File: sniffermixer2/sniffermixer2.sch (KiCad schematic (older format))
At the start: 19 parts

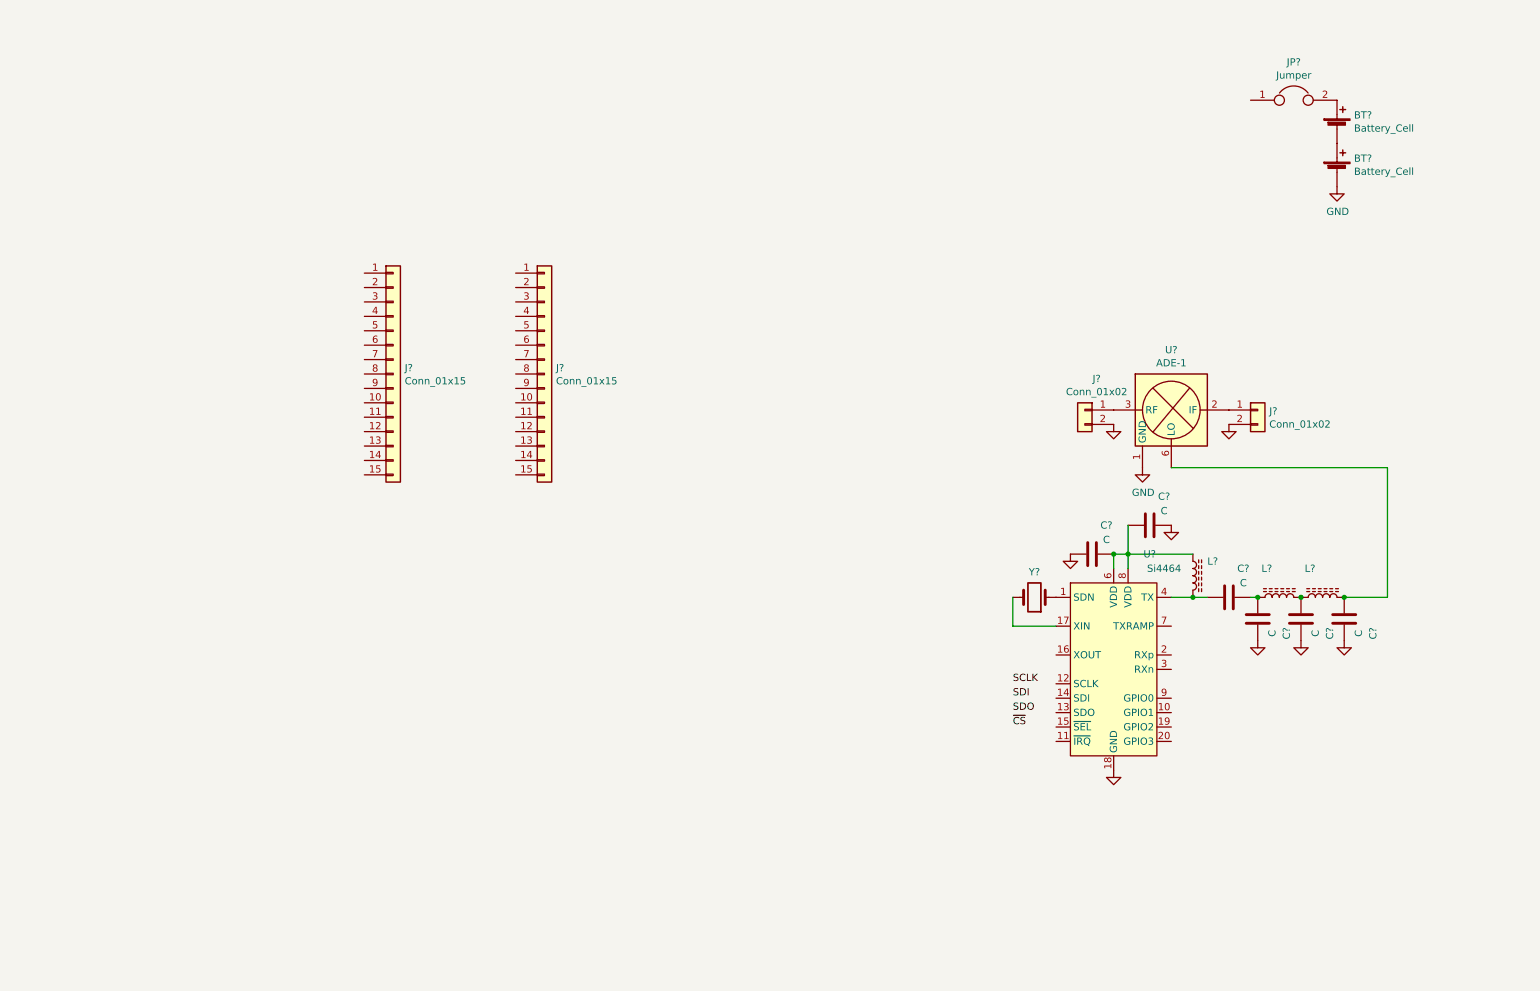
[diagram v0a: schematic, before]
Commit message: some minor schematic capture: dupe connectors, tricolor LED, wiring
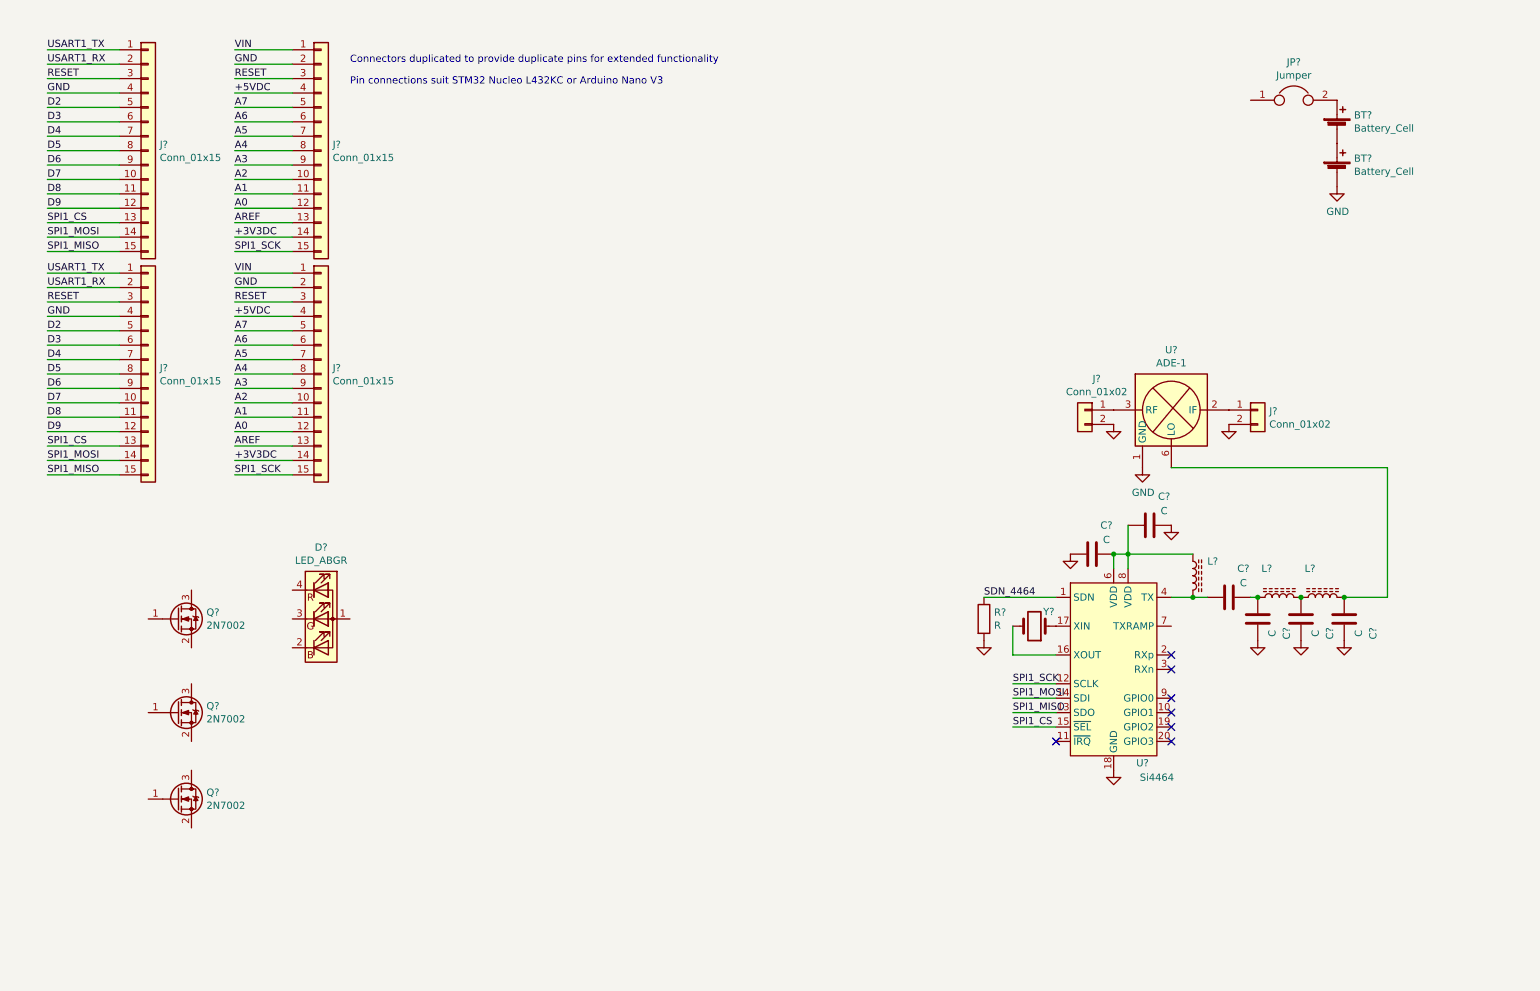
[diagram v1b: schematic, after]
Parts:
- added D?: LED_ABGR, symbol Device:LED_ABGR
- added J? (x2): Conn_01x15, symbol Connector_Generic:Conn_01x15
- added Q? (x3): 2N7002, Package_TO_SOT_SMD:SOT-23, symbol Transistor_FET:2N7002
- added R?: R, symbol Device:R
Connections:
- net GND: now also J?.2 (Pin_2), J?.4 (Pin_4), J?.2 (Pin_2), J?.4 (Pin_4), R?.2
- net at Y?.1: now also U?.17 (XIN); no longer U?.1 (SDN)
- net SPI1_SCK: now reaches U?.12 (SCLK)
- net SPI1_SCK: now also J?.15 (Pin_15), J?.15 (Pin_15)
- net SPI1_MISO: now reaches U?.13 (SDO)
- net SPI1_MISO: now also J?.15 (Pin_15), J?.15 (Pin_15)
- net SPI1_MOSI: now reaches U?.14 (SDI)
- net SPI1_MOSI: now also J?.14 (Pin_14), J?.14 (Pin_14)
- net SPI1_CS: now reaches U?.15 (~SEL)
- net SPI1_CS: now also J?.13 (Pin_13), J?.13 (Pin_13)
- net at U?.16 (XOUT): now also Y?.2
- net USART1_TX: now reaches J?.1 (Pin_1)
- net USART1_TX: now also J?.1 (Pin_1)
- net D7: now reaches J?.10 (Pin_10)
- net D7: now also J?.10 (Pin_10)
- net D8: now reaches J?.11 (Pin_11)
- net D8: now also J?.11 (Pin_11)
- net D9: now reaches J?.12 (Pin_12)
- net D9: now also J?.12 (Pin_12)
- net USART1_RX: now reaches J?.2 (Pin_2)
- net USART1_RX: now also J?.2 (Pin_2)
- net RESET: now reaches J?.3 (Pin_3)
- net RESET: now also J?.3 (Pin_3), J?.3 (Pin_3), J?.3 (Pin_3)
- net D2: now reaches J?.5 (Pin_5)
- net D2: now also J?.5 (Pin_5)
- net D3: now reaches J?.6 (Pin_6)
- net D3: now also J?.6 (Pin_6)
- net D4: now reaches J?.7 (Pin_7)
- net D4: now also J?.7 (Pin_7)
- net D5: now reaches J?.8 (Pin_8)
- net D5: now also J?.8 (Pin_8)
- net D6: now reaches J?.9 (Pin_9)
- net D6: now also J?.9 (Pin_9)
- net VIN: now reaches J?.1 (Pin_1)
- net VIN: now also J?.1 (Pin_1)
- net A2: now reaches J?.10 (Pin_10)
- net A2: now also J?.10 (Pin_10)
- net A1: now reaches J?.11 (Pin_11)
- net A1: now also J?.11 (Pin_11)
- net A0: now reaches J?.12 (Pin_12)
- net A0: now also J?.12 (Pin_12)
- net AREF: now reaches J?.13 (Pin_13)
- net AREF: now also J?.13 (Pin_13)
- net +3V3DC: now reaches J?.14 (Pin_14)
- net +3V3DC: now also J?.14 (Pin_14)
- net +5VDC: now reaches J?.4 (Pin_4)
- net +5VDC: now also J?.4 (Pin_4)
- net A7: now reaches J?.5 (Pin_5)
- net A7: now also J?.5 (Pin_5)
- net A6: now reaches J?.6 (Pin_6)
- net A6: now also J?.6 (Pin_6)
- net A5: now reaches J?.7 (Pin_7)
- net A5: now also J?.7 (Pin_7)
- net A4: now reaches J?.8 (Pin_8)
- net A4: now also J?.8 (Pin_8)
- net A3: now reaches J?.9 (Pin_9)
- net A3: now also J?.9 (Pin_9)
- new net SDN_4464: R?.1, U?.1 (SDN)
- no-connect marks 0 -> 7
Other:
- note added: "Connectors duplicated to provide duplicate pins for extended functionality"
- note added: "Pin connections suit STM32 Nucleo L432KC or Arduino Nano V3"
- moved on the sheet: J?, Y?

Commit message: Revision B hardware finalized and ready for production
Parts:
- removed BT?: Battery_Cell, symbol Device:Battery_Cell
- removed C?: C, symbol Device:C
- removed D?: LED_ABGR, symbol Device:LED_ABGR
- removed J? (x2): Conn_01x02, symbol Connector_Generic:Conn_01x02
- removed JP?: Jumper, symbol Device:Jumper
- removed L?: L_Core_Ferrite, symbol Device:L_Core_Ferrite
- removed Q? (x3): 2N7002, Package_TO_SOT_SMD:SOT-23, symbol Transistor_FET:2N7002
- added C10, C11, C3: 0.1uF, Capacitor_SMD:C_0603_1608Metric, symbol Device:C
- added C2: 330uF, Capacitor_SMD:C_0805_2012Metric, symbol Device:C
- added C5: 22pF, Capacitor_SMD:C_0603_1608Metric, symbol Device:C
- added C9: 1uF, Capacitor_SMD:C_0603_1608Metric, symbol Device:C
- added D1: LED_Dual_ACA, LED_THT:LED_D5.0mm-3, symbol Device:LED_Dual_ACA
- added D2: BAT54A, Package_TO_SOT_SMD:SOT-23, symbol Diode:BAT54A
- added J10, J9: Conn_01x08, Connector_PinHeader_2.54mm:PinHeader_1x08_P2.54mm_Vertical, symbol Connector_Generic:Conn_01x08
- added J11, J8: Conn_01x02, Connector_PinHeader_2.54mm:PinHeader_1x02_P2.54mm_Vertical, symbol Connector_Generic:Conn_01x02
- added J5: USB_B_Micro, Connector_USB:USB_Micro-B_Molex_47346-0001, symbol sniffermixer2-rescue:USB_B_Micro-Connector
- added J6, J7: Conn_Coaxial, Connector_Coaxial:SMA_Amphenol_901-144_Vertical, symbol sniffermixer2-rescue:Conn_Coaxial-Connector
- added L3, L4: 18nH, Inductor_SMD:L_0805_2012Metric_Pad1.15x1.40mm_HandSolder, symbol Device:L_Core_Ferrite
- added L5: 4.7uH, Inductor_SMD:L_0805_2012Metric_Pad1.15x1.40mm_HandSolder, symbol Device:L_Core_Ferrite
- added Q1, Q2: BSS84, Package_TO_SOT_SMD:SOT-23, symbol Transistor_FET:BSS84
- added R1, R2, R9: 1M, Resistor_SMD:R_0603_1608Metric, symbol Device:R
- added R10, R11, R4, R5, R6, R7: DNF, Resistor_SMD:R_0603_1608Metric, symbol Device:R
- added R12, R13: 100k, Resistor_SMD:R_0603_1608Metric, symbol Device:R
- added R8: 1M78, Resistor_SMD:R_0603_1608Metric, symbol Device:R
- added U3: LTC3526, Package_DFN_QFN:DFN-6-1EP_2x2mm_P0.5mm_EP0.61x1.42mm, symbol outside_std_libs_parts:LTC3526
- added X1: TG2520SMN 30MHz TCXO, Oscillator:Oscillator_SMD_SeikoEpson_SG210-4Pin_2.5x2.0mm, symbol Oscillator:SG-210SED
- BT2: renamed from BT?; value Battery_Cell -> LR6/FR6; footprint (none) -> Battery:BatteryHolder_Keystone_2462_2xAA
- C1: renamed from C?; value C -> 10uF; footprint (none) -> Capacitor_SMD:C_0603_1608Metric
- C4: renamed from C?; value C -> 33pF; footprint (none) -> Capacitor_SMD:C_0603_1608Metric
- C6, C8: renamed from C?; value C -> 15pF; footprint (none) -> Capacitor_SMD:C_0603_1608Metric
- C7: renamed from C?; value C -> 8.2pF; footprint (none) -> Capacitor_SMD:C_0603_1608Metric
- J1, J2, J3, J4: renamed from J?; footprint (none) -> Connector_PinHeader_2.54mm:PinHeader_1x15_P2.54mm_Vertical
- L1: renamed from L?; value L_Core_Ferrite -> 220nH; footprint (none) -> Inductor_SMD:L_0805_2012Metric_Pad1.15x1.40mm_HandSolder
- L2: renamed from L?; value L_Core_Ferrite -> 56nH; footprint (none) -> Inductor_SMD:L_0805_2012Metric_Pad1.15x1.40mm_HandSolder
- R3: renamed from R?; value R -> 100k; footprint (none) -> Resistor_SMD:R_0603_1608Metric
- U1: renamed from U?; footprint Package_DFN_QFN:QFN-20-1EP_4x4mm_P0.5mm_EP2.6x2.6mm_ThermalVias -> Package_DFN_QFN:QFN-20-1EP_4x4mm_P0.5mm_EP2.6x2.6mm
- Y1: renamed from Y?; footprint (none) -> Crystal:Crystal_SMD_2520-4Pin_2.5x2.0mm
- gave numbers to parts that had none: 1
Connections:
- net +3V3DC is gone; now on net +3V3: J3.14 (Pin_14), J4.14 (Pin_14)
- net D6 is gone; now on net +5VDC: J1.9 (Pin_9), J2.9 (Pin_9)
- net SDN_4464 is gone; now on net D3: R3.1, U1.1 (SDN)
- net +5VDC: now also J5.1 (VBUS)
- net D4: now also Q2.1 (G), R2.2
- net D5: now also Q1.1 (G), R1.2
- net D7: now also U1.11 (~IRQ)
- net D8: now also U3.4 (~SHDN)
- net D9: now also C11.1, D2.1, R13.2
- net GND: now also C10.1, C11.2, C2.2, C3.1, C9.1, D1.2 (K), J10.1 (Pin_1), J10.2 (Pin_2), J10.3 (Pin_3), J10.4 (Pin_4), J10.5 (Pin_5), J10.6 (Pin_6), J10.7 (Pin_7), J10.8 (Pin_8), J11.2 (Pin_2), J5.5 (GND), J5.6 (Shield), J6.2 (Ext), J7.2 (Ext), J9.1 (Pin_1), J9.2 (Pin_2), J9.3 (Pin_3), J9.4 (Pin_4), J9.5 (Pin_5), J9.6 (Pin_6), J9.7 (Pin_7), J9.8 (Pin_8), R4.1, R5.1, R6.1, R7.1, R9.2, U3.2 (GND), U3.7 (PAD), X1.2 (GND)
- net at BT2.1 (+): now also J8.1 (Pin_1)
- net at U2.2 (IF): now also J7.1 (In)
- net at U2.3 (RF): now also J6.1 (In)
- net at U2.6 (LO): now also L4.2; no longer C8.2
- net at U1.10 (GPIO1): now also R5.2
- net at U1.17 (XIN): now also R10.1, R11.2; no longer Y1.1
- net at U1.19 (GPIO2): now also R6.2
- net at U1.20 (GPIO3): now also R7.2
- net +3V3: now reaches C1.1, C4.2, L1.1, U1.6 (VDD), U1.8 (VDD)
- net +3V3: now also C10.2, C2.1, C3.2, C5.2, Q1.2 (S), Q2.2 (S), R1.1, R12.2, R2.1, R8.1, U3.6 (VOUT), X1.4 (Vcc)
- net at U1.9 (GPIO0): now also R4.2
- net at C7.2, L2.2: now also L3.1
- new net: C8.2, L3.2, L4.1
- new net: R10.2, Y1.1
- new net: D1.1 (A1), Q1.3 (D)
- new net: D1.3 (A2), Q2.3 (D)
- new net: L5.1, U3.1 (SW)
- new net: C9.2, J8.2 (Pin_2), L5.2, U3.3 (VIN)
- new net: C5.1, R8.2, R9.1, U3.5 (FB)
- new net: R11.1, X1.3 (OUT)
- new net: D2.3, J11.1 (Pin_1), R12.1, R13.1
- no-connect marks 7 -> 5
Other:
- note added: "+5VDC Input to Nucleo32 PCB provides 3V3 500mA supply"
- note added: "Dummy resistors for breakout of GPIO if required"
- note added: "Fit either XTAL or TCXO"
- note added: "Frequency selection switch (HW debounce)\n10ms = 100nF * 100k"
- note added: "From external antenna\n"
- note added: "Lumex SSL-LX3059IGW or equiv."
- note added: "OPT PWR SW"
- note added: "To YNG Sniffer\n"
- note added: "USB power attachment event sensing\n"
- note added: "VBAT Disable\n"
- moved on the sheet: BT2, C1, R3, U2, Y1
